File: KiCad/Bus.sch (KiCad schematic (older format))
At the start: 15 parts, among them J201 Bus, U201 ST485C

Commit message: Schematic Version 4 Some Software Changes
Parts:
- removed J201: Bus, Pin_Headers:Pin_Header_Straight_2x05, symbol Conn_02x05_Odd_Even
- removed R201, R203: 1k, Resistors_SMD:R_0805, symbol R
- removed R202: 150, Resistors_THT:R_Axial_DIN0207_L6.3mm_D2.5mm_P7.62mm_Horizontal, symbol R
- added J?: Bus, Connectors_IDC:IDC-Header_2x03_Pitch2.54mm_Straight, symbol Conn_02x03_Odd_Even
- added JP1: COMMA PU, SMD_Jumper:Jumper_SMD_02, symbol Jumper_NO_Small
- added JP2: TERM, SMD_Jumper:Jumper_SMD_02, symbol Jumper_NO_Small
- added JP3: COMMB PD, SMD_Jumper:Jumper_SMD_02, symbol Jumper_NO_Small
- added R1, R3: 1k, Resistors_SMD:R_0805, symbol R
- added R2: 150, Resistors_THT:R_Axial_DIN0207_L6.3mm_D2.5mm_P7.62mm_Horizontal, symbol R
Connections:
- net +5V: now also R1.1
- net COMM_A: now also J?.4 (Pin_4), J?.5 (Pin_5), JP1.2, R2.1
- net COMM_B: now also J?.2 (Pin_2), J?.3 (Pin_3), JP2.2, JP3.1
- net GND: now also J?.1 (Pin_1), J?.6 (Pin_6), R3.2
- new net: JP1.1, R1.2
- new net: JP2.1, R2.2
- new net: JP3.2, R3.1
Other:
- note added: "Erster und letzter Teilnehmer am Bus \nbenötigen eine Abschlussimpedanz\nBei Flachbandkabel zwischen \n100Ω und 200Ω (differentiell).\nAngegeben: 104Ω (AWG 28, GSG)."
- note removed: "Erster und letzter Teilnehmer am Bus \nbenötigen eine Abschlussimpedanz\nBei Flachbandkabel zwischen \n100Ω und 200Ω (differentiell).\nAngegeben: 104Ω (AWG 28, GSG).\nKann evtl. über Klemmleiste oder\nPinheader befestigt werden."
- note removed: "Spannungsversorgung und Bus \nüber 10 Pol Flachbandkabel, \neinmal rund ums Spielfeld. \nAuswerteeinheit (1x pro Spielfeld) \nspeist Spannungsversorgung ein \nund bildet Schnittstelle zur \nAuswertung und Datenübergabe\nbzw. Einstellung."
- moved on the sheet: C201, R204, U201

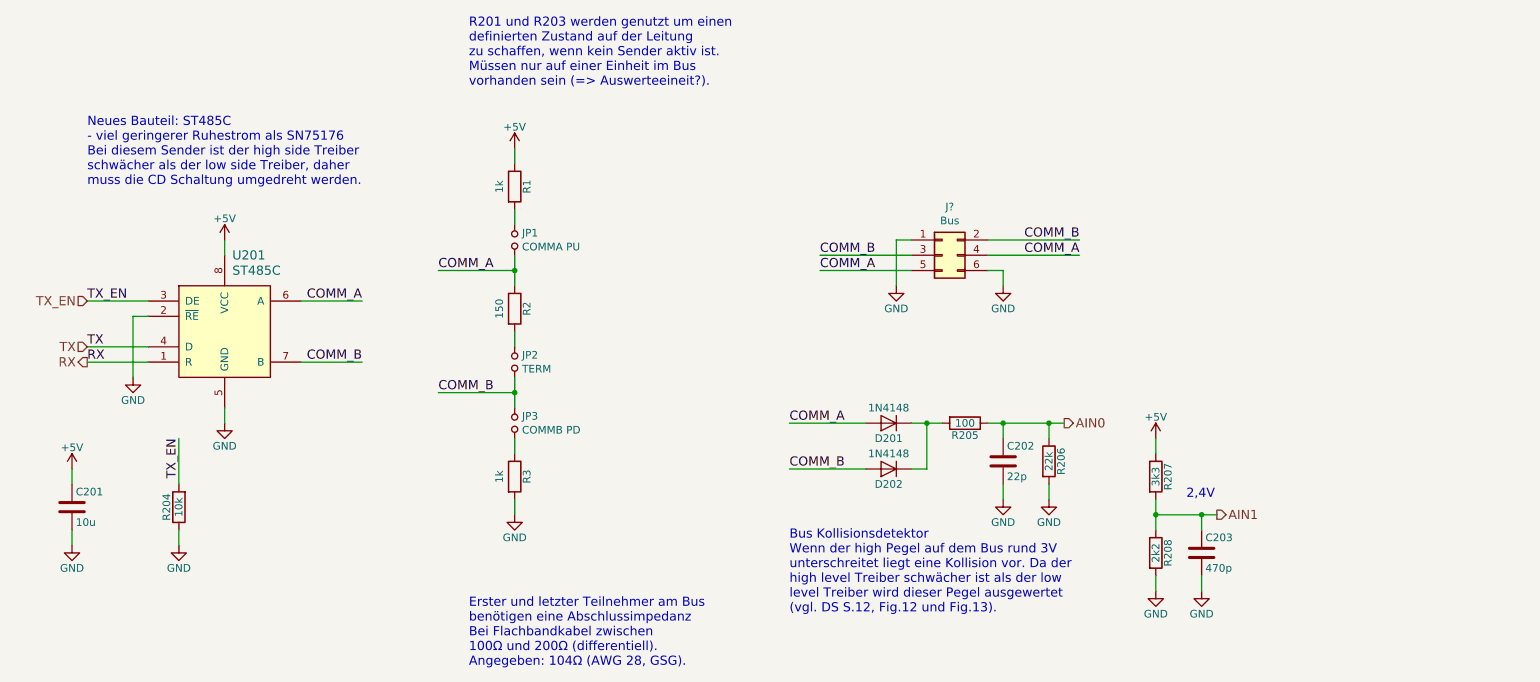
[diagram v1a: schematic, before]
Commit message: Changes to V4 Schematic, new Board design
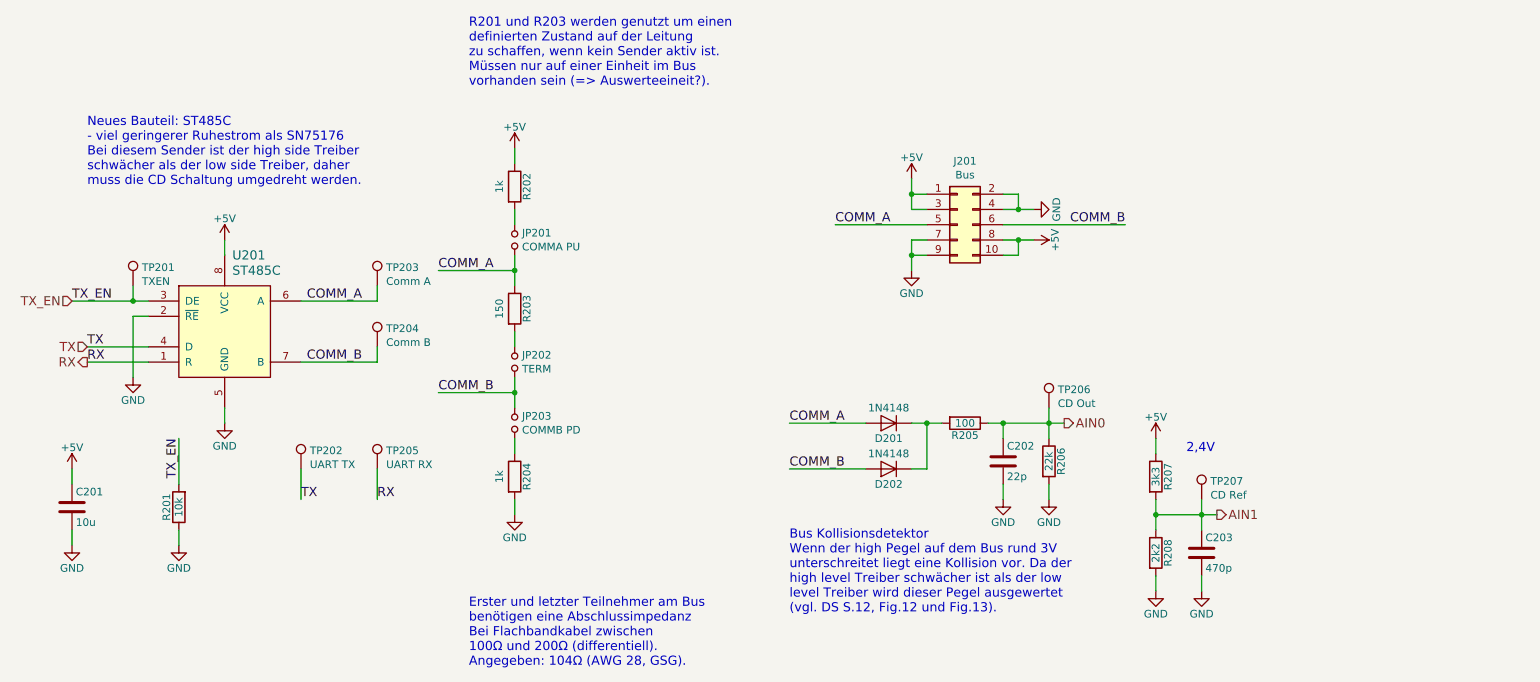
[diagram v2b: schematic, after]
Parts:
- removed J?: Bus, Connectors_IDC:IDC-Header_2x03_Pitch2.54mm_Straight, symbol Conn_02x03_Odd_Even
- added J201: Bus, Connectors_IDC:IDC-Header_2x05_Pitch2.54mm_Straight, symbol Conn_02x05_Odd_Even
- added TP201: TXEN, Test:TEST_10, symbol Test_Point
- added TP202: UART TX, Test:TEST_10, symbol Test_Point
- added TP203: Comm A, Test:TEST_10, symbol Test_Point
- added TP204: Comm B, Test:TEST_10, symbol Test_Point
- added TP205: UART RX, Test:TEST_10, symbol Test_Point
- added TP206: CD Out, Test:TEST_10, symbol Test_Point
- added TP207: CD Ref, Test:TEST_10, symbol Test_Point
- R203: renamed from R2; footprint Resistors_THT:R_Axial_DIN0207_L6.3mm_D2.5mm_P7.62mm_Horizontal -> Resistors_SMD:R_0805
- renumbered JP1 to JP201, JP2 to JP202, JP3 to JP203, R204 to R201, R1 to R202, R3 to R204
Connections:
- net +5V: now also J201.1 (Pin_1), J201.10 (Pin_10), J201.3 (Pin_3), J201.8 (Pin_8)
- net AIN0: now also TP206.1
- net AIN1: now also TP207.1
- net COMM_A: now also J201.5 (Pin_5), TP203.1
- net COMM_B: now also J201.6 (Pin_6), TP204.1
- net GND: now also J201.2 (Pin_2), J201.4 (Pin_4), J201.7 (Pin_7), J201.9 (Pin_9)
- net RX: now also TP205.1
- net TX: now also TP202.1
- net TX_EN: now also TP201.1
